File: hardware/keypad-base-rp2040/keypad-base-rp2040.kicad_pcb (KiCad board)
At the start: 2 copper layers, 150.2 x 64.2 mm, 64 parts, among them J1 USB_C_Receptacle_USB2.0, J3 Conn_02x05_SWD, Q1 AO3400A, SW1 Switch_SW_Push, SW2 Switch_SW_Push, SW3 Switch_SW_Push, SW4 Switch_SW_Push, SW5 Switch_SW_Push, SW6 Switch_SW_Push, SW7 Switch_SW_Push, SW8 Switch_SW_Push, SW9 Switch_SW_Push, U1 RP2040, U10 AP2112K-3.3, U11 W25Q128JVS, U3 IE096HQ1301CL, U4 IE096HQ1301CL, U5 IE096HQ1301CL, U6 IE096HQ1301CL, U7 IE096HQ1301CL, U8 IE096HQ1301CL, X1 12MHz

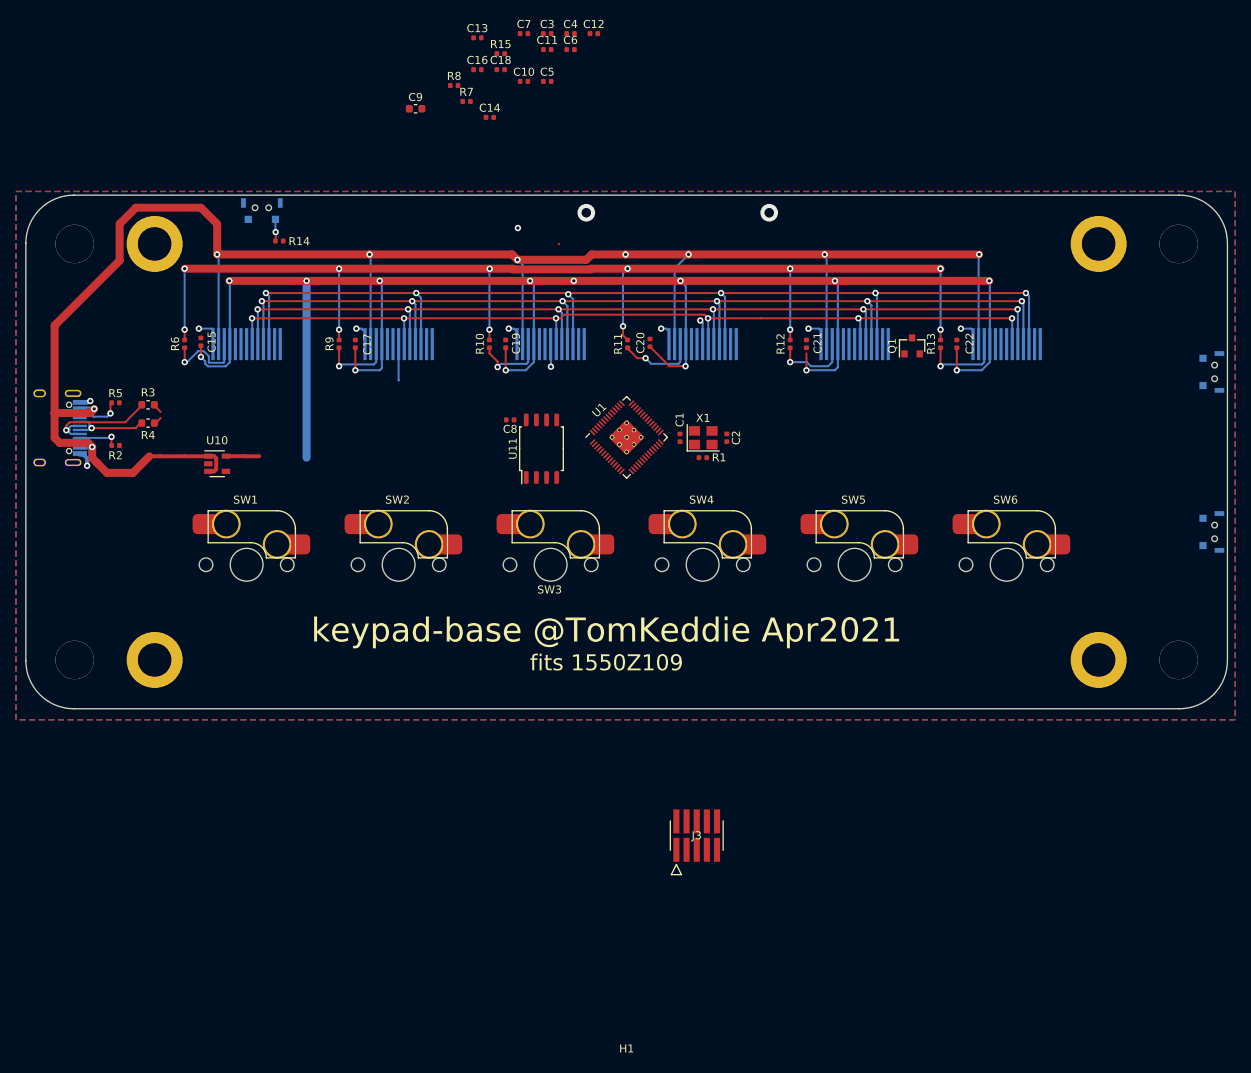
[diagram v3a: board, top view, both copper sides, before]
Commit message: hardware/keypad-base-rp2040: placed, routed, ERC & DRC clean
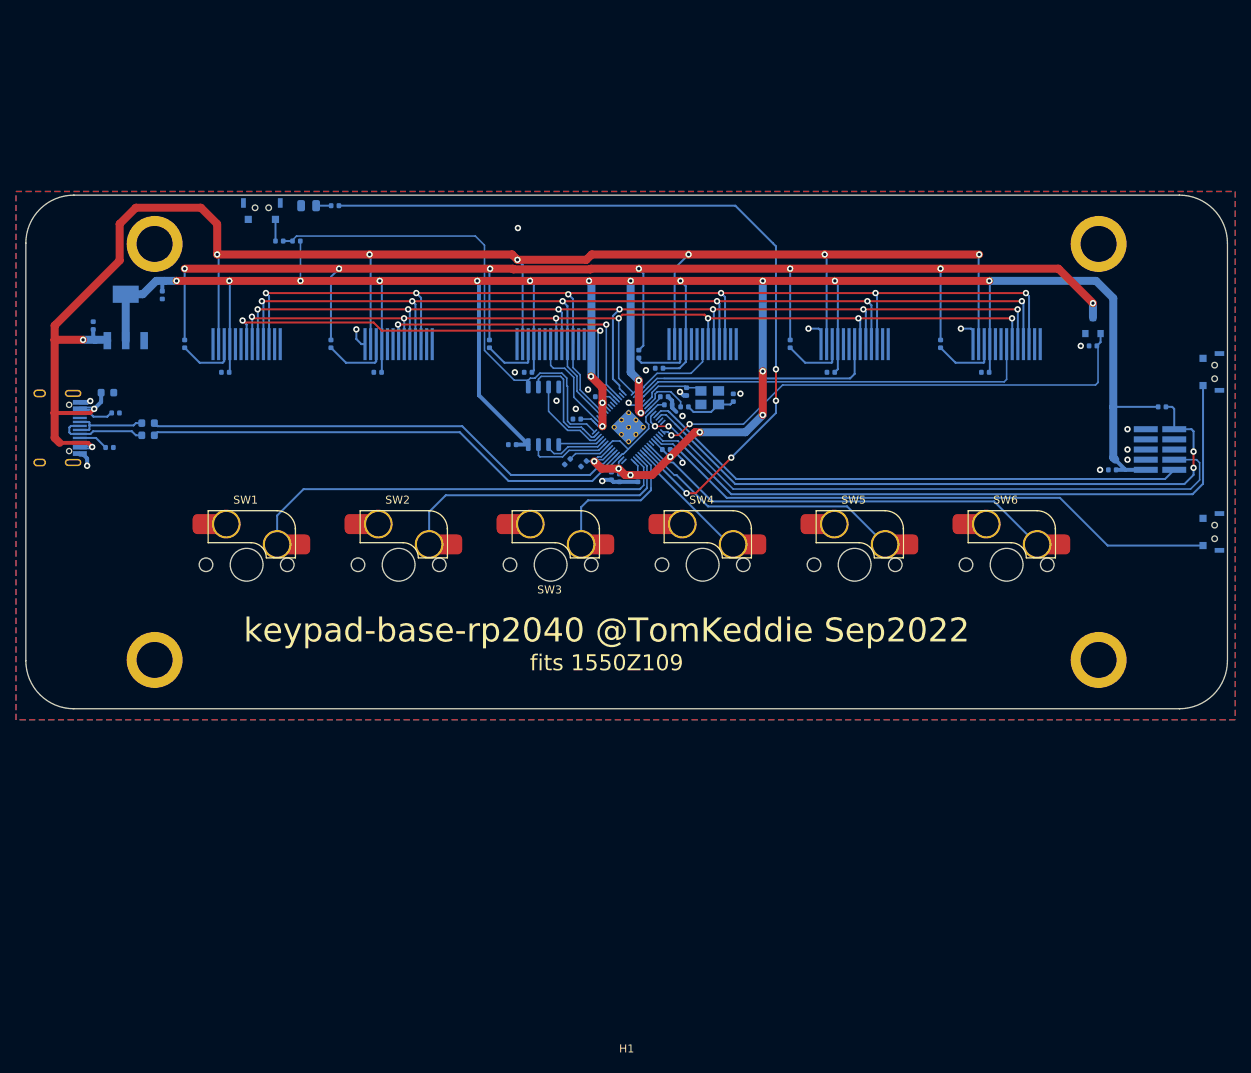
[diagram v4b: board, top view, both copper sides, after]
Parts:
- removed U10: AP2112K-3.3, tom-semiconductors:SOT-23-5
- added C23: 2.2uF,6.3V,X5R, tom-passives:C_0402_1005Metric, B.Cu at (165.6, 89.2)
- added D1: LED, tom-opto:LED_0805_2012Metric, B.Cu at (126.7, 55.1)
- added R16: 470, tom-passives:R_0402_1005Metric, B.Cu at (130.0, 55.1)
- added VR1: LM1117MPX-3.3, tom-semiconductors:VREG_LM1117MPX-3.3, B.Cu at (103.9, 69.1)
- C1, C10, C11, C12, C13, C14, C15, C16, C17, C18, C19, C2, C20, C21, C22, C3, C4, C5, C6, C7, C8, C9, J3, Q1, R1, R10, R11, R12, R13, R14, R15, R2, R3, R4, R5, R6, R7, R8, R9, U1, U11, X1: moved to B.Cu
- moved R7 94.9 mm to (233.4, 80.3)
- moved C10 88.1 mm to (227.2, 88.1), turned to 180 degrees
- moved R15 82.5 mm to (224.8, 72.6), turned to 180 degrees
- moved J3 75.4 mm to (233.2, 85.6), turned to 90 degrees
- moved C13 58.6 mm to (167.9, 89.2), turned to -90 degrees
- moved C16 57.7 mm to (99.8, 70.1), turned to 90 degrees
- moved C3 53.6 mm to (159.1, 87.1), turned to -135 degrees
- moved C12 52.8 mm to (171.4, 85.6)
- moved C9 52.4 mm to (101.6, 78.5)
- moved C18 50.8 mm to (108.5, 66.3), turned to -90 degrees
- moved C5 50.0 mm to (164.6, 88.9), turned to -90 degrees
- moved C4 48.0 mm to (171.7, 80.0)
- moved C7 46.3 mm to (163.1, 79.0), turned to 180 degrees
- moved C6 46.2 mm to (160.3, 81.8), turned to 180 degrees
- moved C11 45.8 mm to (171.2, 79.0)
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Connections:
- U1 pad 11: /SW1 -> /~{CS1}
- U1 pad 12: /SW2 -> /~{CS2}
- U1 pad 13: /SW3 -> unconnected-(U1-Pad13)
- U1 pad 14: /SW4 -> /D\C
- U1 pad 15: /SW5 -> /~{LCDRESET}
- U1 pad 16: /SW6 -> /~{CS4}
- U1 pad 17: /SW7 -> /~{CS5}
- U1 pad 18: /SW8 -> /~{CS6}
- U1 pad 2: unconnected-(U1-Pad2) -> /~{CS3}
- U1 pad 29: unconnected-(U1-Pad29) -> /BACKLIGHT
- U1 pad 31: /~{LCDRESET} -> /SW8
- U1 pad 32: /BACKLIGHT -> /SW7
- U1 pad 34: /D\C -> unconnected-(U1-Pad34)
- U1 pad 35: /~{CS6} -> /SW6
- U1 pad 36: /~{CS5} -> /SW5
- U1 pad 37: unconnected-(U1-Pad37) -> Net-(R16-Pad1)
- U1 pad 38: /~{CS4} -> /SW4
- U1 pad 39: /~{CS3} -> /SW3
- U1 pad 40: /~{CS2} -> /SW2
- U1 pad 41: /~{CS1} -> /SW1
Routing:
- net +3.3V: track 222.8 -> 365.3 mm, vias 14 -> 24
- net Net-(R16-Pad1): track 0.00 -> 100.5 mm, vias 0 -> 4
- net /SW8: track 0.00 -> 83.9 mm
- net /~{RESET}: track 0.00 -> 82.8 mm, vias 0 -> 2
- net /SWCLK: track 0.00 -> 79.3 mm, vias 0 -> 2
- net /SW7: track 0.00 -> 73.9 mm
- net /SWD: track 0.00 -> 69.0 mm
- net /BACKLIGHT: track 0.00 -> 63.5 mm, vias 0 -> 2
- net /QSPI_SS: track 0.00 -> 61.8 mm
- net /USB_P: track 0.00 -> 61.4 mm
- net /USB_N: track 0.91 -> 62.0 mm
- net /~{CS1}: track 0.00 -> 58.1 mm, vias 0 -> 2
- net /SW1: track 2.39 -> 57.1 mm
- net /SW6: track 2.94 -> 56.0 mm
- net /~{CS6}: track 0.01 -> 51.3 mm
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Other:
- board text added: "keypad-base-rp2040 @TomKeddie Sep2022"
- board text removed: "keypad-base @TomKeddie Apr2021"

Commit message: hardare/keypad-base-rp2040: Sep2022 as submitted
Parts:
- added TP1: TestPoint, tom-mechanical:TestPoint_Pad_D1.0mm, F.Cu at (162.1, 78.2)
- moved H1 46.2 mm to (165.6, 113.8)
- moved C7 0.83 mm to (163.2, 78.2), turned to 135 degrees
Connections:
- U1 pad 6: unconnected-(U1-Pad6) -> Net-(TP1-Pad1)
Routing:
- net Net-(TP1-Pad1): track 0.00 -> 4.50 mm, vias 0 -> 1
- net GND: vias 22 -> 38
